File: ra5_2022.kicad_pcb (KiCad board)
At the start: 2 copper layers, 80.5 x 45 mm, 160 parts, among them CN1 KF250-3.5-2P-2, CN2 MX15EDGRHC-3.5-2*02P-BK01-CU-A, CN3 KF250-3.5-2P-2, CN4 KF250-3.5-2P-2, J1 Bus_M.2_Socket_E, J2 Conn_01x04_Socket, J3 MX15EDGRHC-3.5-2x03P, Q1 BC817, Q2 BC817, Q3 BC817, Q4 BC817, Q5 BC817, U1 STM8S003F3P, U10 ATM90E32AS-AU-R, U11 K3-2268P, U12 ADS1115IDGS, U2 TPS54202DDC, U3 B0303S-1WR2, U4 JTD6206-3.3V, U5 ISO7741N1-Y, U6 CS817X20LS, U7 AMS1117-3.3, U8 DB126V-5.0-2P-BK-P, U9 DB126V-5.0-2P-BK-P, Y1 ABM8G-16.384MHZ-18-D2Y-T

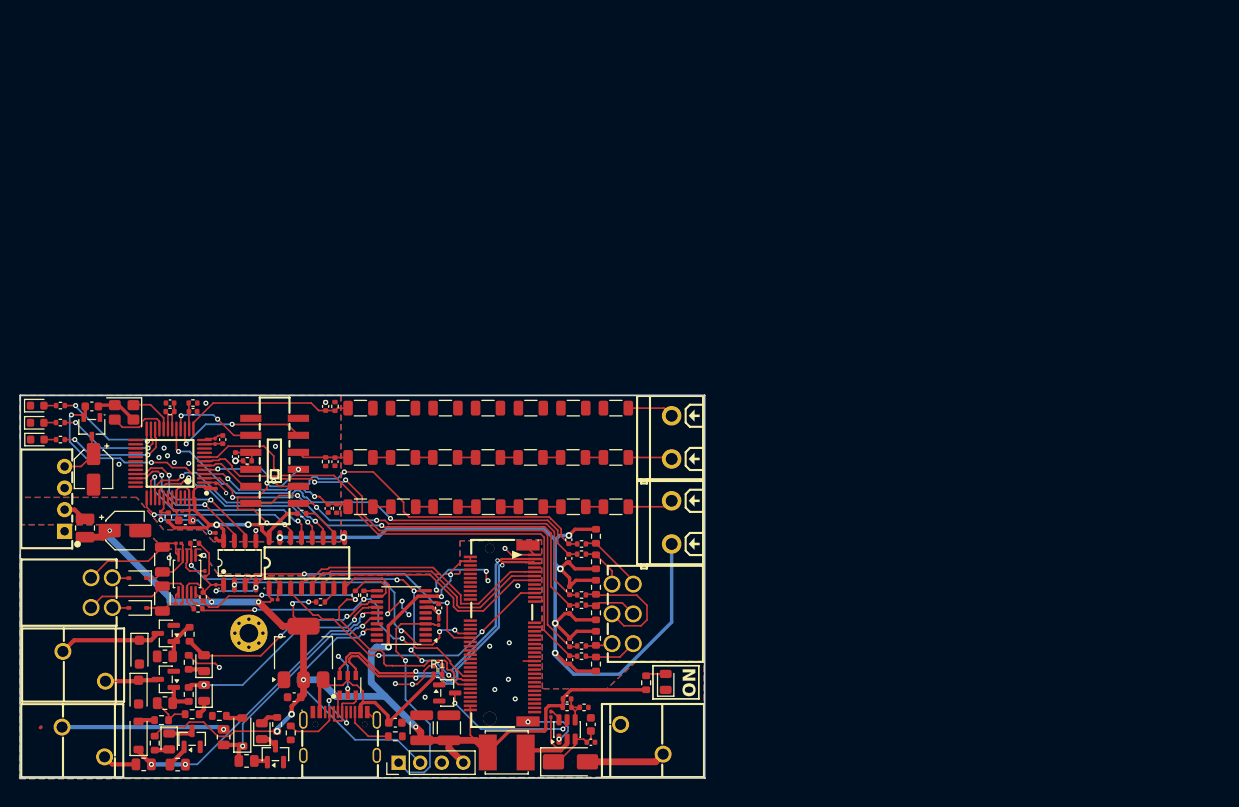
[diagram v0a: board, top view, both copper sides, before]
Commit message: Migra componentes das bibliotecas LCSC locais para pecas JLCPCB
Troca os part numbers para casar com o estoque da JLCPCB e com o
catalogo PCBA Basic, eliminando a biblioteca local que era importada
via easyeda2kicad.

- Remove libraries/ (simbolos, footprints e modelos 3D importados) e o
  script import_lcsc_component.sh
- Adiciona o plugin JLCPCB (jlcpcb/project.db) e os scripts auxiliares
  fix_jlcpcb_tools_deps.sh e generate_ibom.sh
- Atualiza as cinco folhas do esquematico, o PCB e as regras de projeto

O PCB fica em estado intermediario: os componentes novos ainda precisam
ser reposicionados e as trilhas refeitas.

Co-Authored-By: Claude Opus 5 (1M context) <noreply@anthropic.com>
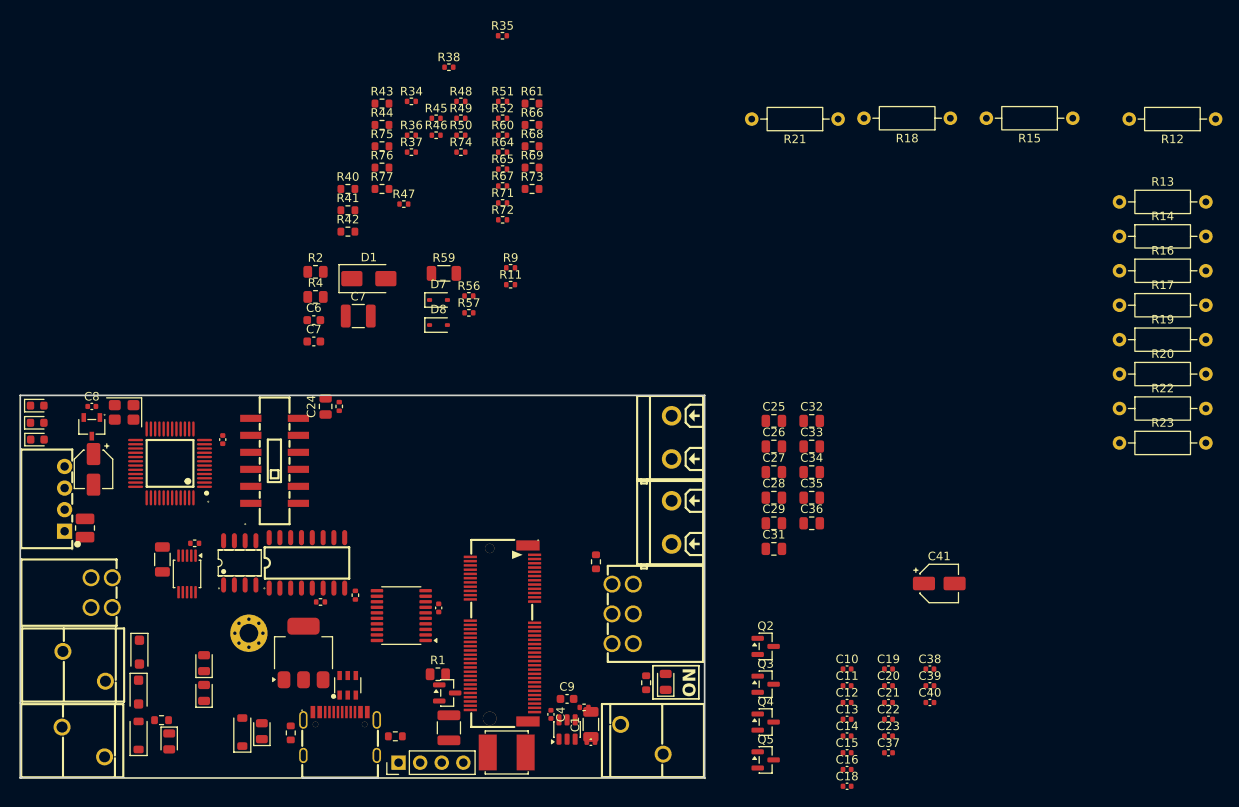
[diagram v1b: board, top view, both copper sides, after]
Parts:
- removed C3: 10uF, Capacitor_SMD:CP_Elec_4x5.4
- removed the C7 at (155.7, 112.8)
- removed R24, R25, R26, R27, R28, R29, R30, R31, R32: 12M, Resistor_SMD:R_1206_3216Metric
- removed R53: 270R, Resistor_SMD:R_0402_1005Metric
- removed R54: 10k, Resistor_SMD:R_0402_1005Metric
- removed R63, R70: 1K, Resistor_SMD:R_0603_1608Metric
- removed the REF** at (158.8, 79.6)
- added C41: 10uF, Capacitor_SMD:CP_Elec_4x5.4, F.Cu at (216.6, 95.8)
- added C6: 22uF, Capacitor_SMD:C_0603_1608Metric, F.Cu at (143.0, 64.8)
- added C7: 22uF, Capacitor_SMD:C_1210_3225Metric, F.Cu at (148.2, 64.4)
- added C7: 22uF, Capacitor_SMD:C_0603_1608Metric, F.Cu at (143.0, 67.4)
- added R74: 10k, Resistor_SMD:R_0402_1005Metric, F.Cu at (160.3, 45.1)
- added R75: 270R, Resistor_SMD:R_0603_1608Metric, F.Cu at (151.0, 44.4)
- added R76: 270R, Resistor_SMD:R_0603_1608Metric, F.Cu at (151.0, 46.9)
- added R77: 270R, Resistor_SMD:R_0603_1608Metric, F.Cu at (151.0, 49.4)
- C1: footprint Capacitor_SMD:C_0603_1608Metric -> Capacitor_SMD:C_1206_3216Metric
- C10, C12, C14, C15, C16, C18, C19, C20, C21, C23, C37, C38, C39, C4, C40: footprint Capacitor_SMD:C_0201_0603Metric -> Capacitor_SMD:C_0402_1005Metric
- C11, C13, C22, C8: footprint Capacitor_SMD:C_0603_1608Metric -> Capacitor_SMD:C_0402_1005Metric
- C24, C25, C26, C27, C28, C29, C31, C32, C33, C34, C35, C36: footprint Capacitor_SMD:C_0402_1005Metric -> Capacitor_SMD:C_0805_2012Metric
- C9: footprint Capacitor_SMD:C_0402_1005Metric -> Capacitor_SMD:C_0603_1608Metric
- D1: value SS16 -> SS210
- D7, D8: value SD103AWS -> 1N5819WS
- J3: value MX15EDGRHC-3.5-2x03P -> MX15EDGRHC-3.5-2*03P-BK01-Cu-A
- Q1, Q2, Q3, Q4, Q5: value BC817 -> BC817-25
- R1, R2, R4: footprint Resistor_SMD:R_0402_1005Metric -> Resistor_SMD:R_0805_2012Metric
- R12, R13, R14, R15, R16, R17, R18, R19, R20, R21, R22, R23: value 12M -> 120k; footprint Resistor_SMD:R_1206_3216Metric -> Resistor_THT:R_Axial_DIN0207_L6.3mm_D2.5mm_P10.16mm_Horizontal
- R5: value 22.1k -> 22k
- R51, R52: value 270R -> 1k
- R60, R64, R65, R67, R71, R72: footprint Resistor_SMD:R_0805_2012Metric -> Resistor_SMD:R_0402_1005Metric
- U4: value JTD6206-3.3V -> XC6206P332MR-JSM
- U6: value CS817X20LS -> CA-IS3720CLS
- moved C37 90.1 mm to (210.6, 115.7), turned to 0 degrees
- moved C39 89.9 mm to (215.5, 107.9)
- moved C40 89.1 mm to (215.5, 109.8), turned to 0 degrees
- moved C23 86.5 mm to (210.6, 113.8), turned to 0 degrees
- moved C21 86.4 mm to (210.6, 109.8), turned to 0 degrees
- moved C38 86.0 mm to (215.5, 105.9), turned to 0 degrees
- moved C22 86.0 mm to (210.6, 111.8), turned to 0 degrees
- moved R60 85.2 mm to (165.2, 43.1)
- moved R66 85.2 mm to (168.7, 41.9), turned to 0 degrees
- moved C20 84.5 mm to (210.6, 107.9)
- moved R61 82.2 mm to (168.7, 39.4), turned to 0 degrees
- moved C19 82.0 mm to (210.6, 105.9), turned to 0 degrees
- moved R65 79.8 mm to (165.2, 47.1)
- moved R12 78.3 mm to (249.1, 41.2)
- moved C14 77.9 mm to (205.7, 113.8), turned to 0 degrees
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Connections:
- C10 pad 1: GND -> VDD
- C10 pad 2: VDD -> GND
- C11 pad 1: GND -> +5V_USB
- C11 pad 2: +5V_USB -> GND
- C12 pad 1: GND -> VDD
- C12 pad 2: VDD -> GND
- C13 pad 1: GND -> VDD
- C13 pad 2: VDD -> GND
- C14 pad 1: GND2 -> VDD2
- C14 pad 2: VDD2 -> GND2
- C15 pad 1: GND2 -> VDD2
- C15 pad 2: VDD2 -> GND2
- C19 pad 1: GND2 -> VDD2
- C19 pad 2: VDD2 -> GND2
- C20 pad 1: GND2 -> VDD2
- C20 pad 2: VDD2 -> GND2
- C21 pad 1: GND2 -> /MCU/M90E32AS/VDD18
- C21 pad 2: /MCU/M90E32AS/VDD18 -> GND2
- C22 pad 1: GND2 -> /MCU/M90E32AS/VDD18
- C22 pad 2: /MCU/M90E32AS/VDD18 -> GND2
- C23 pad 1: GND2 -> /MCU/M90E32AS/VREF
- C23 pad 2: /MCU/M90E32AS/VREF -> GND2
- C31 pad 1: /MCU/M90E32AS/I1P -> GND2
- C31 pad 2: GND2 -> /MCU/M90E32AS/I1N
- C32 pad 1: GND2 -> /MCU/M90E32AS/I2P_SW
- C32 pad 2: /MCU/M90E32AS/I1N -> GND2
- C33 pad 1: /MCU/M90E32AS/I2P_SW -> GND2
- C33 pad 2: GND2 -> /MCU/M90E32AS/I2N_SW
- C34 pad 1: GND2 -> /MCU/M90E32AS/I3P
- C34 pad 2: /MCU/M90E32AS/I2N_SW -> GND2
- C35 pad 1: /MCU/M90E32AS/I3P -> GND2
- C35 pad 2: GND2 -> /MCU/M90E32AS/I3N
- C36 pad 1: GND2 -> /MCU/M90E32AS/I1P
- C36 pad 2: /MCU/M90E32AS/I3N -> GND2
- C37 pad 1: GND2 -> /MCU/M90E32AS/~RESET
- C37 pad 2: /MCU/M90E32AS/~RESET -> GND2
- C38 pad 1: GND -> VDD
- C38 pad 2: VDD -> GND
- C39 pad 1: /MCU/Analog IO/AIN1 -> /MCU/Analog IO/AIN0
- C39 pad 2: /MCU/Analog IO/AIN0 -> /MCU/Analog IO/AIN1
- C40 pad 1: /MCU/Analog IO/AIN2- -> /MCU/Analog IO/AIN2
- C40 pad 2: /MCU/Analog IO/AIN2 -> /MCU/Analog IO/AIN2-
- D7 pad 1: /MCU/Analog IO/AIN0 -> /MCU/Analog IO/AIN2
- D7 pad 2: /MCU/Analog IO/AIN1+ -> /MCU/Analog IO/AIN2+
- D8 pad 1: /MCU/Analog IO/AIN2 -> /MCU/Analog IO/AIN0
- D8 pad 2: /MCU/Analog IO/AIN2+ -> /MCU/Analog IO/AIN1+
- R2 pad 1: Net-(Q1-B) -> GND
- R2 pad 2: GND -> Net-(Q1-B)
- R21 pad 2: Net-(R21-Pad2) -> /MCU/M90E32AS/V1P
- R22 pad 2: Net-(R22-Pad2) -> /MCU/M90E32AS/V2P_SW
- R23 pad 2: Net-(R23-Pad2) -> /MCU/M90E32AS/V3P
- R4 pad 1: VDD -> /Power Source/FB
- R4 pad 2: /Power Source/FB -> VDD
- R51 pad 1: /MCU/M90E32AS/ZX0 -> /MCU/Digital IO/DO1_MCU
- R51 pad 2: Net-(D4-A) -> Net-(Q2-B)
- R52 pad 1: /MCU/M90E32AS/ZX1 -> /MCU/Digital IO/DO2_MCU
- R52 pad 2: Net-(D5-A) -> Net-(Q4-B)
- R56 pad 1: /MCU/SDA -> unconnected-(R56-Pad1)
- R56 pad 2: VDD -> unconnected-(R56-Pad2)
- R60 pad 1: /MCU/Digital IO/DI1 -> /MCU/Digital IO/DIN1_MCU
- R60 pad 2: /MCU/Digital IO/DIN1_MCU -> /MCU/Digital IO/DI1
- R66 pad 1: Net-(D11-A) -> VDD
- R66 pad 2: VDD -> Net-(D11-A)
- R67 pad 1: /MCU/Digital IO/DI2 -> /MCU/Digital IO/DIN2_MCU
- R67 pad 2: /MCU/Digital IO/DIN2_MCU -> /MCU/Digital IO/DI2
- R68 pad 1: Net-(D13-K) -> VDD
- R68 pad 2: GND -> Net-(D15-A)
- R73 pad 1: Net-(D15-A) -> Net-(D13-K)
- R73 pad 2: VDD -> GND
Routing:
- net VDD: track 169.1 -> 0.00 mm, vias 12 -> 0
- net GND2: track 153.7 -> 0.00 mm, vias 24 -> 0
- net GND: track 75.8 -> 0.00 mm, vias 26 -> 0
- net /MCU/M90E32AS/I3N: track 62.8 -> 0.00 mm
- net /MCU/M90E32AS/I3P: track 60.8 -> 0.00 mm, vias 2 -> 0
- net VDD2: track 55.0 -> 0.00 mm, vias 4 -> 0
- net /MCU/M90E32AS/I1N: track 50.6 -> 0.00 mm, vias 2 -> 0
- net /MCU/M90E32AS/I1P: track 50.0 -> 0.00 mm, vias 2 -> 0
- net /MCU/M90E32AS/I2N_SW: track 47.8 -> 0.00 mm, vias 2 -> 0
- net /MCU/ALERT: track 47.2 -> 0.00 mm, vias 6 -> 0
- net /MCU/SCL: track 44.4 -> 0.00 mm, vias 2 -> 0
- net /MCU/M90E32AS/I2P_SW: track 40.5 -> 0.00 mm, vias 2 -> 0
- net /MCU/SDA: track 39.8 -> 0.00 mm, vias 3 -> 0
- net /MCU/USB_DP: track 37.6 -> 0.00 mm, vias 2 -> 0
- net /MCU/USB_DN: track 36.9 -> 0.00 mm, vias 2 -> 0
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- removed copper zone on B.Cu, net GND
- removed copper zone on F.Cu, net GND
- removed copper zone on B.Cu, net GND2
- removed copper zone on F.Cu, net GND2

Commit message: Reintroduz biblioteca local ra5_2022 e atualiza layout/esquematicos
Volta a usar simbolos, footprints e modelos 3D importados via
easyeda2kicad (libraries/) em vez das pecas basicas JLCPCB adotadas no
commit anterior, alem de atualizar o roteamento/posicionamento no PCB
e as cinco folhas do esquematico.

Co-Authored-By: Claude Sonnet 5 <noreply@anthropic.com>
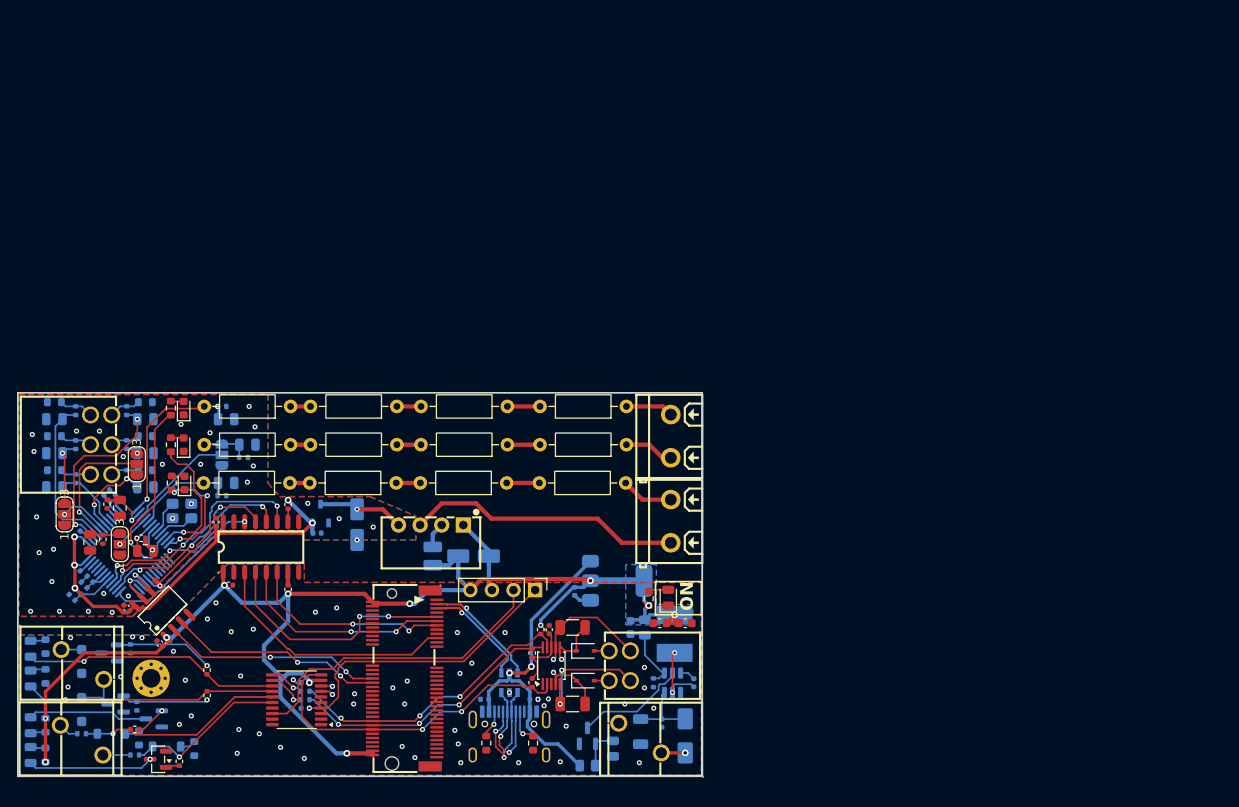
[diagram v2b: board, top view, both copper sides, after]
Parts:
- removed the C6 at (158.9, 112.8)
- removed the C7 at (148.2, 64.4)
- removed U11: K3-2268P, ra5_2022:SW-SMD_12P-L14.9-W4.9_K3-2268P
- added C42: 10uF, Capacitor_SMD:C_0402_1005Metric, B.Cu at (168.9, 109.5)
- added JP1: SolderJumper_3_Open, Jumper:SolderJumper-3_P1.3mm_Open_RoundedPad1.0x1.5mm_NumberLabels, B.Cu at (132.2, 80.7)
- added JP2: SolderJumper_3_Open, Jumper:SolderJumper-3_P1.3mm_Open_RoundedPad1.0x1.5mm_NumberLabels, F.Cu at (120.2, 91.2)
- added JP3: SolderJumper_3_Open, Jumper:SolderJumper-3_P1.3mm_Open_RoundedPad1.0x1.5mm_NumberLabels, F.Cu at (122.2, 81.8)
- added JP4: SolderJumper_3_Open, Jumper:SolderJumper-3_P1.3mm_Open_RoundedPad1.0x1.5mm_NumberLabels, F.Cu at (113.7, 87.7)
- C1, C11, C13, C16, C17, C18, C19, C2, C20, C21, C22, C23, C24, C26, C28, C30, C31, C32, C33, C34, C35, C36, C37, C39, C4, C40, C41, C5, C8, C9, D1, D10, D11, D12, D13, D14, D15, D16, D3, D9, L1, L2, Q1, Q2, Q4, Q5, R1, R10, R11, R2, R33, R35, R37, R39, R4, R40, R41, R42, R43, R44, R45, R46, R47, R48, R49, R5, R50, R60, R61, R62, R64, R66, R67, R68, R69, R71, R73, R74, U10, U2, U4, U7, USB1, Y1: moved to B.Cu
- moved C37 97.8 mm to (114.6, 97.5), turned to 135 degrees
- moved R23 97.7 mm to (140.2, 84.0), turned to 180 degrees
- moved R22 97.6 mm to (140.3, 79.5), turned to 180 degrees
- moved C19 96.7 mm to (115.2, 90.0), turned to 180 degrees
- moved C20 96.4 mm to (115.2, 94.0)
- moved C22 95.9 mm to (116.0, 96.0), turned to 135 degrees
- moved C23 95.4 mm to (119.4, 85.8), turned to 45 degrees
- moved C21 95.0 mm to (116.7, 95.3), turned to 135 degrees
- moved R66 93.6 mm to (111.5, 116.0), turned to 90 degrees
- moved C35 89.1 mm to (112.5, 84.5)
- moved C33 89.1 mm to (112.5, 80.5)
- moved R68 89.0 mm to (111.5, 112.5), turned to -90 degrees
- moved R61 88.4 mm to (111.5, 106.8), turned to -90 degrees
- moved C14 86.1 mm to (121.0, 98.7), turned to 135 degrees
- moved R20 86.0 mm to (152.7, 84.0), turned to 180 degrees
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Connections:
- J3 pad 1: /MCU/M90E32AS/IT+ -> /MCU/M90E32AS/IR+
- J3 pad 2: /MCU/M90E32AS/IT- -> /MCU/M90E32AS/IR-
- J3 pad 5: /MCU/M90E32AS/IR+ -> /MCU/M90E32AS/IT+
- J3 pad 6: /MCU/M90E32AS/IR- -> /MCU/M90E32AS/IT-
- R56 pad 1: unconnected-(R56-Pad1) -> /MCU/SDA
- R56 pad 2: unconnected-(R56-Pad2) -> VDD
- U1 pad 15: /MCU/Digital IO/DIN1_MCU -> /MCU/Digital IO/DIN2_MCU
- U1 pad 16: /MCU/Digital IO/DIN2_MCU -> /MCU/Digital IO/DIN1_MCU
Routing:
- net VDD: track 0.00 -> 164.6 mm, vias 0 -> 12
- net GND2: track 0.00 -> 57.1 mm, vias 0 -> 27
- net VDD2: track 0.00 -> 52.5 mm, vias 0 -> 5
- net +5V_USB: track 0.00 -> 39.6 mm, vias 0 -> 2
- net /MCU/ALERT: track 0.00 -> 39.6 mm, vias 0 -> 2
- net /MCU/SWIM: track 0.00 -> 37.0 mm
- net /MCU/SDA: track 0.00 -> 34.8 mm, vias 0 -> 3
- net /MCU/NRST: track 0.00 -> 34.6 mm, vias 0 -> 1
- net /MCU/SCL: track 0.00 -> 32.5 mm, vias 0 -> 3
- net /MCU/Digital IO/DO2_MCU: track 0.00 -> 30.3 mm, vias 0 -> 1
- net /MCU/CS: track 0.00 -> 29.8 mm
- net /MCU/Digital IO/DO1_MCU: track 0.00 -> 29.5 mm, vias 0 -> 1
- net /MCU/SCLK: track 0.00 -> 29.0 mm, vias 0 -> 2
- net /MCU/M90E32AS/MISO: track 0.00 -> 27.2 mm, vias 0 -> 3
- net /MCU/PM0: track 0.00 -> 25.7 mm, vias 0 -> 2
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- added copper zone on B.Cu, net GND
- added copper zone on F.Cu, net GND
- added copper zone on B.Cu, net GND2
- added copper zone on F.Cu, net GND2
- added copper zone on B.Cu, net VDD
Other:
- board size 80.5 x 45 mm -> 80.5 x 45.1 mm
- board text removed: "+"
- board text removed: "-"
- board text removed: "AIN1"
- board text removed: "AIN2"
- board text removed: "DIN1"
- board text removed: "DIN2"
- board text removed: "DOUT1"
- board text removed: "DOUT2"
- board text removed: "GND"
- board text removed: "VCC"
